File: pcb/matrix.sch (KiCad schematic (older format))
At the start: 143 parts

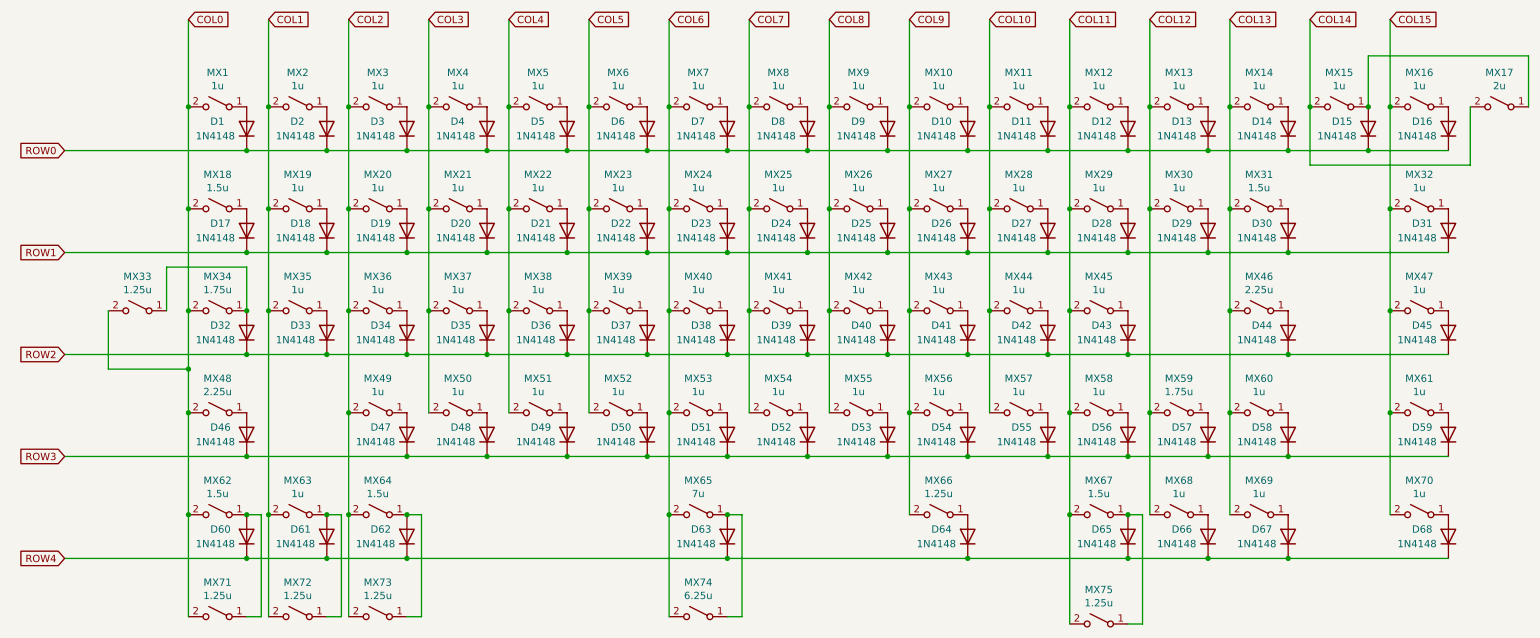
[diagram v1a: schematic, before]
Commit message: Added hotswap
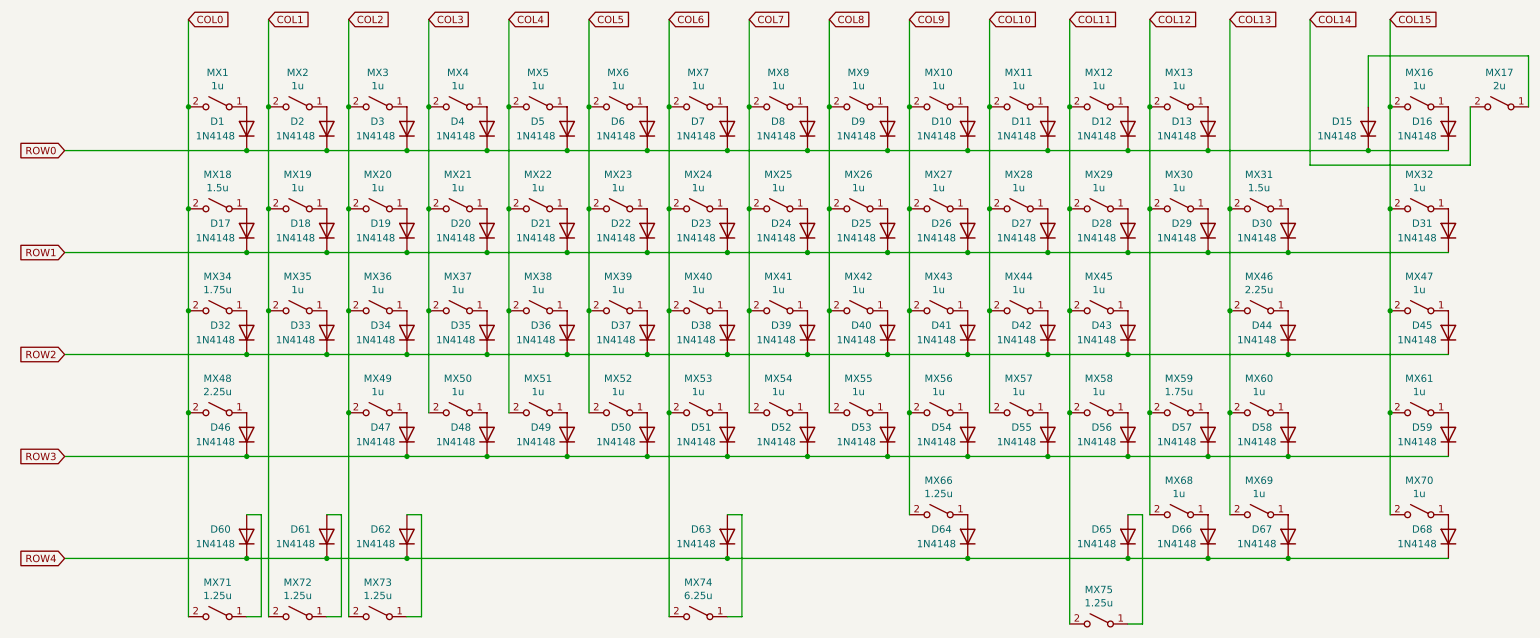
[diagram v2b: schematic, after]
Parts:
- removed D14: 1N4148, Diode_SMD:D_SOD-123, symbol Device:D
- removed MX14, MX15, MX63: 1u, MX_Only:MXOnly-1U-NoLED, symbol Switch:SW_SPST
- removed MX33: 1.25u, MX_Only:MXOnly-1.25U-NoLED, symbol Switch:SW_SPST
- removed MX62, MX64, MX67: 1.5u, MX_Only:MXOnly-1.5U-NoLED, symbol Switch:SW_SPST
- removed MX65: 7u, MX_Only:MXOnly-7U-ReversedStabilizers-NoLED, symbol Switch:SW_SPST
- MX1, MX10, MX11, MX12, MX13, MX16, MX19, MX2, MX20, MX21, MX22, MX23, MX24, MX25, MX26, MX27, MX28, MX29, MX3, MX30, MX32, MX35, MX36, MX37, MX38, MX39, MX4, MX40, MX41, MX42, MX43, MX44, MX45, MX47, MX49, MX5, MX50, MX51, MX52, MX53, MX54, MX55, MX56, MX57, MX58, MX6, MX60, MX61, MX68, MX69, MX7, MX70, MX8, MX9: footprint MX_Only:MXOnly-1U-NoLED -> MechKeys:Kailh_socket_MX
- MX17: footprint MX_Only:MXOnly-2U-NoLED -> MX_Only:MXOnly-2U-Hotswap
- MX18, MX31: footprint MX_Only:MXOnly-1.5U-NoLED -> MX_Only:MXOnly-1.5U-Hotswap
- MX34, MX59: footprint MX_Only:MXOnly-1.75U-NoLED -> MX_Only:MXOnly-1.75U-Hotswap
- MX46, MX48: footprint MX_Only:MXOnly-2.25U-NoLED -> MX_Only:MXOnly-2.25U-Hotswap
- MX66, MX71, MX72, MX73, MX75: footprint MX_Only:MXOnly-1.25U-NoLED -> MX_Only:MXOnly-1.25U-Hotswap
- MX74: footprint MX_Only:MXOnly-6.25U-ReversedStabilizers-NoLED -> MX_Only:MXOnly-6.25U-Hotswap-ReversedStabilizers
